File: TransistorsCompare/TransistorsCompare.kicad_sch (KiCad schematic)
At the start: 14 parts, among them J1 Conn_01x02_Socket, J2 Conn_01x02_Socket, J3 NPN, J4 NPN, J5 Conn_01x01_MountingPin, J6 Conn_01x01_MountingPin, U1 TL084

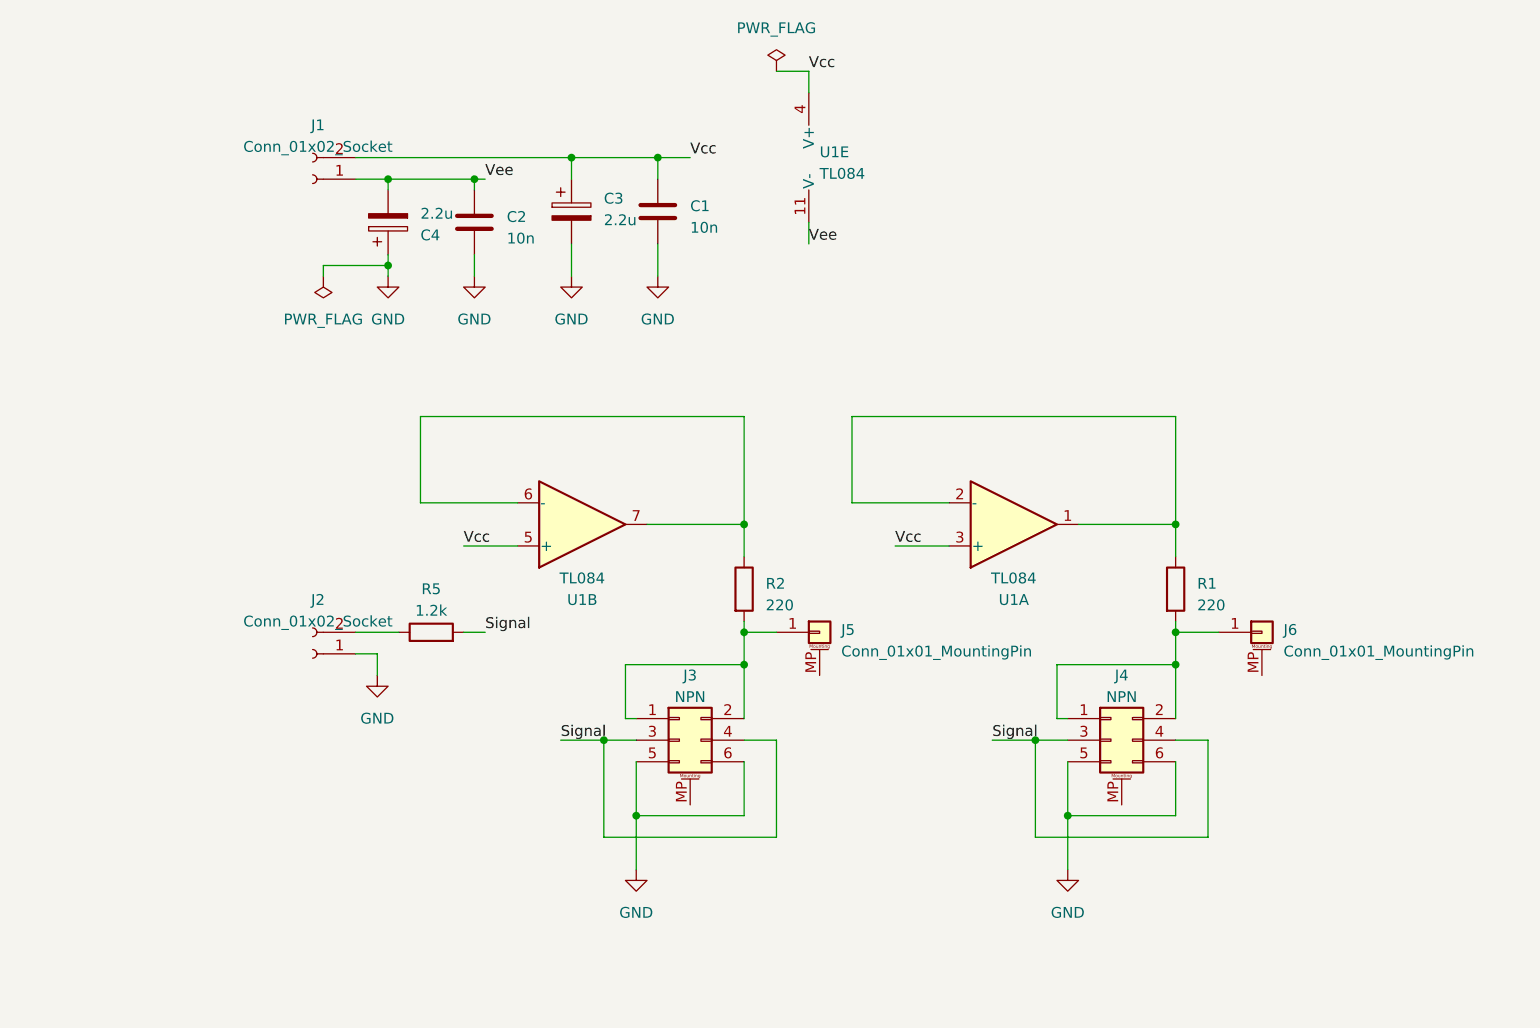
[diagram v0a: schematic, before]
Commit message: fix : all thrue one AOP
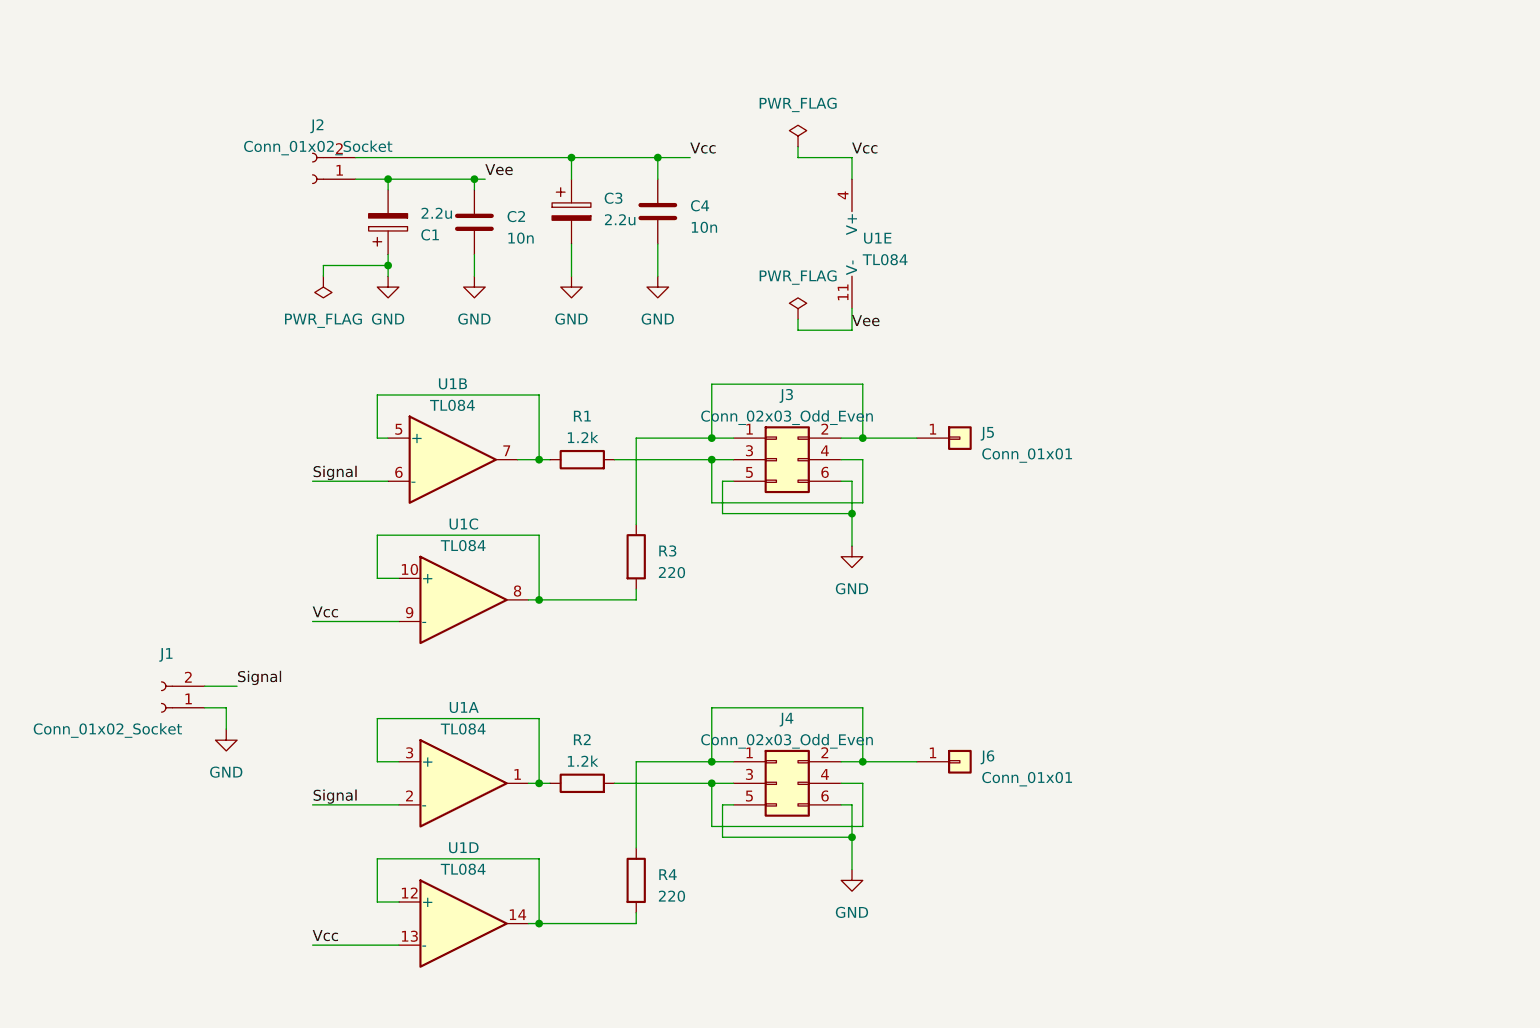
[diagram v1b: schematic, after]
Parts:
- removed J3, J4: NPN, Connector_PinSocket_2.54mm:PinSocket_2x03_P2.54mm_Vertical, symbol Connector_Generic_MountingPin:Conn_02x03_Odd_Even_MountingPin
- removed J5, J6: Conn_01x01_MountingPin, Connector_PinHeader_2.54mm:PinHeader_1x01_P2.54mm_Vertical, symbol Connector_Generic_MountingPin:Conn_01x01_MountingPin
- added J3, J4: Conn_02x03_Odd_Even, Connector_PinSocket_2.54mm:PinSocket_2x03_P2.54mm_Vertical, symbol Connector_Generic:Conn_02x03_Odd_Even
- added J5, J6: Conn_01x01, Connector_PinHeader_2.54mm:PinHeader_1x01_P2.54mm_Vertical, symbol Connector_Generic:Conn_01x01
- added R2: 1.2k, Resistor_THT:R_Axial_DIN0207_L6.3mm_D2.5mm_P10.16mm_Horizontal, symbol Device:R
- added unit 3 of U1
- added unit 4 of U1
- renumbered C4 to C1, C1 to C4, J2 to J1, J1 to J2, R5 to R1, R2 to R3, R1 to R4
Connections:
- net GND: now also J3.5 (Pin_5), J3.6 (Pin_6), J4.5 (Pin_5), J4.6 (Pin_6)
- net Signal: now also J1.2 (Pin_2), U1.2 (-), U1.6 (-); no longer R1.2
- net Vcc: now also U1.13 (-), U1.9 (-); no longer U1.3 (+), U1.5 (+)
- net at R4.2: now also U1.12 (+), U1.14
- net at R1.1: now also U1.5 (+), U1.7; no longer J1.2 (Pin_2)
- net at R3.2: now also U1.10 (+), U1.8
- new net: R2.1, U1.1, U1.3 (+)
- new net: J4.3 (Pin_3), J4.4 (Pin_4), R2.2
- new net: J4.1 (Pin_1), J4.2 (Pin_2), J6.1 (Pin_1), R4.1
- new net: J3.1 (Pin_1), J3.2 (Pin_2), J5.1 (Pin_1), R3.1
- new net: J3.3 (Pin_3), J3.4 (Pin_4), R1.2
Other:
- moved on the sheet: J1, R1, R3, R4

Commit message: T compare
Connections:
- net Signal: now also U1.3 (+), U1.5 (+); no longer U1.2 (-), U1.6 (-)
- net Vcc: now also U1.10 (+), U1.12 (+); no longer U1.13 (-), U1.9 (-)
- net at R2.1, U1.1: now also U1.2 (-); no longer U1.3 (+)
- net at R4.2, U1.14: now also U1.13 (-); no longer U1.12 (+)
- net at R3.2, U1.8: now also U1.9 (-); no longer U1.10 (+)
- net at R1.1, U1.7: now also U1.6 (-); no longer U1.5 (+)
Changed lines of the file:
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@@
     )
   )
-  (symbol (lib_id "Amplifier_Operational:TL084") (at 93.98 85.09 0) (unit 3)
-    (in_bom yes) (on_board yes) (dnp no) (fields_autoplaced)
-    (property "Reference" "U1" (at 93.98 76.2 0)
-      (effects (font (size 1.27 1.27)))
-    )
-    (property "Value" "TL084" (at 93.98 78.74 0)
-      (effects (font (size 1.27 1.27)))
-    )
-    (property "Footprint" "Package_DIP:DIP-14_W7.62mm_Socket" (at 92.71 82.55 0)
-      (effects (font (size 1.27 1.27)) hide)
-    )
-    (property "Datasheet" "http://www.ti.com/lit/ds/symlink/tl081.pdf" (at 95.25 80.01 0)
+  (symbol (lib_id "Amplifier_Operational:TL084") (at 93.98 85.09 0) (mirror x) (unit 3)
+    (in_bom yes) (on_board yes) (dnp no)
+    (property "Reference" "U1" (at 93.98 93.98 0)
+      (effects (font (size 1.27 1.27)))
+    )
+    (property "Value" "TL084" (at 93.98 91.44 0)
+      (effects (font (size 1.27 1.27)))
+    )
+    (property "Footprint" "Package_DIP:DIP-14_W7.62mm_Socket" (at 92.71 87.63 0)
+      (effects (font (size 1.27 1.27)) hide)
+    )
+    (property "Datasheet" "http://www.ti.com/lit/ds/symlink/tl081.pdf" (at 95.25 90.17 0)
       (effects (font (size 1.27 1.27)) hide)
     )
@@
     )
   )
-  (symbol (lib_id "Amplifier_Operational:TL084") (at 92.71 68.58 0) (unit 2)
-    (in_bom yes) (on_board yes) (dnp no) (fields_autoplaced)
-    (property "Reference" "U1" (at 92.71 59.69 0)
-      (effects (font (size 1.27 1.27)))
-    )
-    (property "Value" "TL084" (at 92.71 62.23 0)
-      (effects (font (size 1.27 1.27)))
-    )
-    (property "Footprint" "Package_DIP:DIP-14_W7.62mm_Socket" (at 91.44 66.04 0)
-      (effects (font (size 1.27 1.27)) hide)
-    )
-    (property "Datasheet" "http://www.ti.com/lit/ds/symlink/tl081.pdf" (at 93.98 63.5 0)
+  (symbol (lib_id "Amplifier_Operational:TL084") (at 92.71 68.58 0) (mirror x) (unit 2)
+    (in_bom yes) (on_board yes) (dnp no)
+    (property "Reference" "U1" (at 92.71 77.47 0)
+      (effects (font (size 1.27 1.27)))
+    )
+    (property "Value" "TL084" (at 92.71 74.93 0)
+      (effects (font (size 1.27 1.27)))
+    )
+    (property "Footprint" "Package_DIP:DIP-14_W7.62mm_Socket" (at 91.44 71.12 0)
+      (effects (font (size 1.27 1.27)) hide)
+    )
+    (property "Datasheet" "http://www.ti.com/lit/ds/symlink/tl081.pdf" (at 93.98 73.66 0)
       (effects (font (size 1.27 1.27)) hide)
     )
@@
     )
   )
-  (symbol (lib_id "Amplifier_Operational:TL084") (at 93.98 106.68 0) (unit 1)
-    (in_bom yes) (on_board yes) (dnp no) (fields_autoplaced)
-    (property "Reference" "U1" (at 93.98 97.79 0)
-      (effects (font (size 1.27 1.27)))
-    )
-    (property "Value" "TL084" (at 93.98 100.33 0)
-      (effects (font (size 1.27 1.27)))
-    )
-    (property "Footprint" "Package_DIP:DIP-14_W7.62mm_Socket" (at 92.71 104.14 0)
-      (effects (font (size 1.27 1.27)) hide)
-    )
-    (property "Datasheet" "http://www.ti.com/lit/ds/symlink/tl081.pdf" (at 95.25 101.6 0)
+  (symbol (lib_id "Amplifier_Operational:TL084") (at 93.98 106.68 0) (mirror x) (unit 1)
+    (in_bom yes) (on_board yes) (dnp no)
+    (property "Reference" "U1" (at 93.98 115.57 0)
+      (effects (font (size 1.27 1.27)))
+    )
+    (property "Value" "TL084" (at 93.98 113.03 0)
+      (effects (font (size 1.27 1.27)))
+    )
+    (property "Footprint" "Package_DIP:DIP-14_W7.62mm_Socket" (at 92.71 109.22 0)
+      (effects (font (size 1.27 1.27)) hide)
+    )
+    (property "Datasheet" "http://www.ti.com/lit/ds/symlink/tl081.pdf" (at 95.25 111.76 0)
       (effects (font (size 1.27 1.27)) hide)
     )
@@
     )
   )
-  (symbol (lib_id "Amplifier_Operational:TL084") (at 93.98 123.19 0) (unit 4)
-    (in_bom yes) (on_board yes) (dnp no) (fields_autoplaced)
-    (property "Reference" "U1" (at 93.98 114.3 0)
-      (effects (font (size 1.27 1.27)))
-    )
-    (property "Value" "TL084" (at 93.98 116.84 0)
-      (effects (font (size 1.27 1.27)))
-    )
-    (property "Footprint" "Package_DIP:DIP-14_W7.62mm_Socket" (at 92.71 120.65 0)
-      (effects (font (size 1.27 1.27)) hide)
-    )
-    (property "Datasheet" "http://www.ti.com/lit/ds/symlink/tl081.pdf" (at 95.25 118.11 0)
-      (effects (font (size 1.27 1.27)) hide)
-    )
+  (symbol (lib_id "Amplifier_Operational:TL084") (at 93.98 123.19 0) (mirror x) (unit 4)
+    (in_bom yes) (on_board yes) (dnp no)
+    (property "Reference" "U1" (at 93.98 132.08 0)
+      (effects (font (size 1.27 1.27)))
+    )
+    (property "Value" "TL084" (at 93.98 129.54 0)
+      (effects (font (size 1.27 1.27)))
+    )
+    (property "Footprint" "Package_DIP:DIP-14_W7.62mm_Socket" (at 92.71 125.73 0)
+      (effects (font (size 1.27 1.27)) hide)
+    )
+    (property "Datasheet" "http://www.ti.com/lit/ds/symlink/tl081.pdf" (at 95.25 128.27 0)
+      (effects (font (size 1.27 1.27)) hide)
+    )
